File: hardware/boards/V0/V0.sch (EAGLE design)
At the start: 157 parts, among them IC2 TPS6300, J12 3.5mm TRRS Jack, J2 HIROSE_DM3BT-DSF-PEJSHIROSE_D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, J3 MOLEX_105450-0101MOLEX_105450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, Q2 ON_SEMI_MMBT5551LT1GON_SEMI_M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, U1 VS1053-L, U2 MICROCHIP_MCP73831T-2ATI-OTMI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, X3 FH12-45S-0.5SH

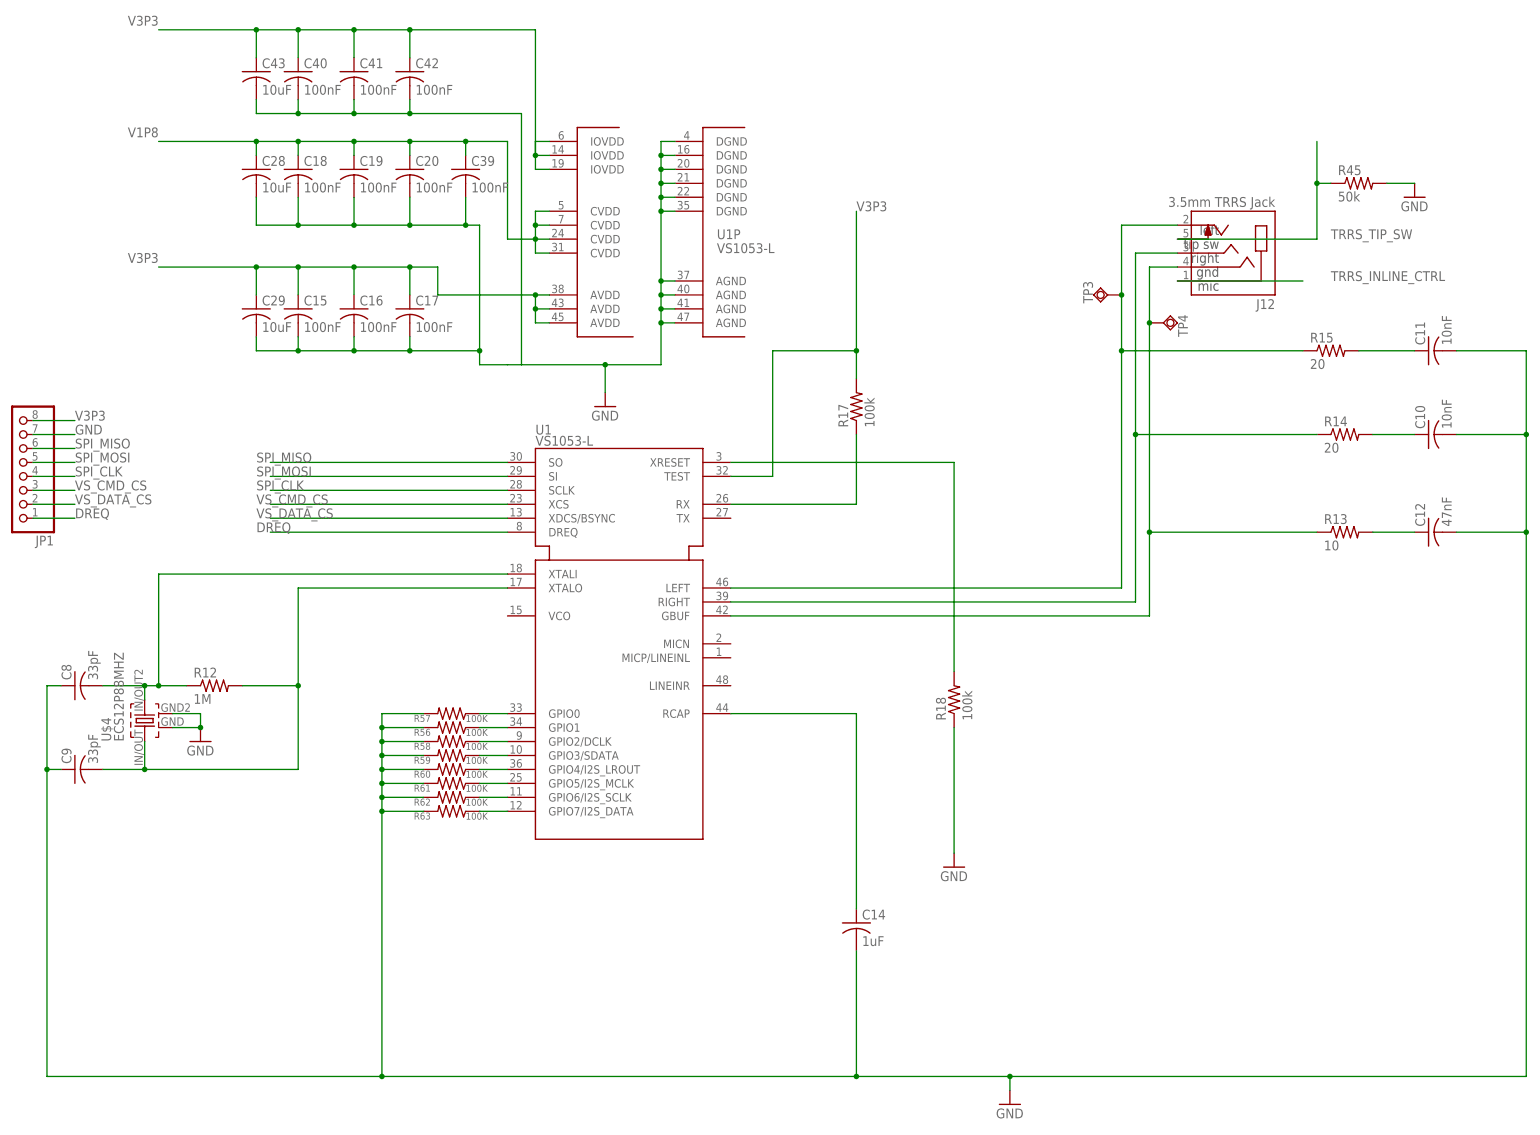
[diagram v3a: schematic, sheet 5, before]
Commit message: VS1053 changes
Switch back to bridging all the GPIO pins (the datasheet's sample connection diagram has it wired this way, so it'll hopefully not be an issue) and tie xRESET to V3P3 (pull-up) so that we can actually boot.
The Adafruit VS1053 breakout schematic mentions that they tie xRESET to low (pull-down) to avoid transients (clicks) in the headphone outputs (as per [this](http://www.vlsi.fi/uploads/media/vs10XXan.pdf)) - making the MCU enable the VS1053 some time after system power up apparently helps mitigate this. Adafruit goes a step further and says that not doing this can "damage the earphones", but since we're pretty heavily pin starved we'll have to risk it.

At this point we seem to match Adafruit's VS1053 breakout in most of the relevant ways. The main (relevant) differences are that we don't differentiate between AGND and GND (or have ferrite beads between them), don't have pull-ups on our CS pins (though this is probably okay since the ESP32 [supposedly doesn't need external pull-ups on its SPI CS pins](https://esp32.com/viewtopic.php?t=3650)), don't have the 2nd set of capacitors/resistors on our right/left output lines (ESD?), and don't have what looks to be a bypass cap and a pull-up (??) resistor on xRESET (peculiar since there's a pull-down resistor on the other side of the level shifter for this pin).

Anyways, we should be in decent shape and we've got the header pins as an escape hatch in case things don't work out.
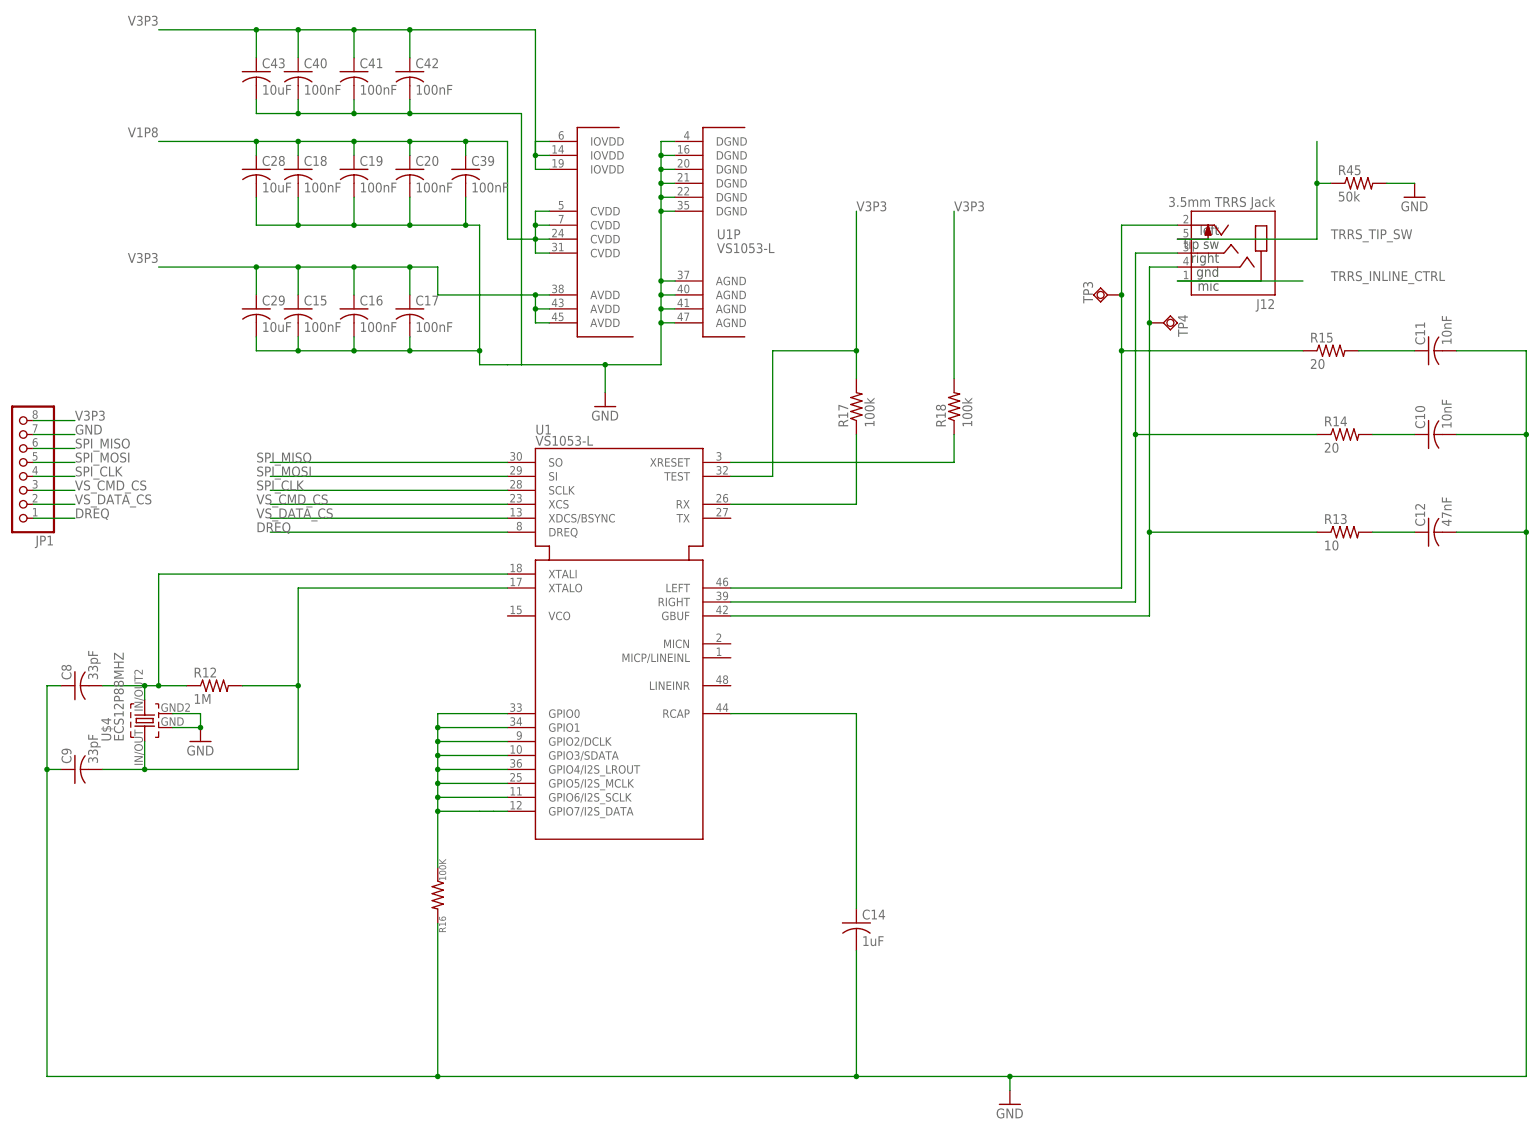
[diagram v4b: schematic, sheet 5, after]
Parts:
- removed R56, R57, R58, R59, R60, R61, R62, R63: 100K, rcl:R-US_R0402
- added R16: 100K, rcl:R-US_R0402
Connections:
- removed net N$13: R58.1, U1G$1.GPIO2/DCLK
- removed net N$15: R59.1, U1G$1.GPIO3/SDATA
- removed net N$17: R60.1, U1G$1.GPIO4/I2S_LROUT
- removed net N$38: R61.1, U1G$1.GPIO5/I2S_MCLK
- removed net N$44: R62.1, U1G$1.GPIO6/I2S_SCLK
- removed net N$7: R57.1, U1G$1.GPIO0
- removed net N$9: R56.1, U1G$1.GPIO1
- net GND: now also R16.2; no longer R18.1, R56.2, R57.2, R58.2, R59.2, R60.2, R61.2, R62.2, R63.2
- net N$41: now also R18.1; no longer R18.2
- net N$45: now also R16.1, U1G$1.GPIO0, U1G$1.GPIO1, U1G$1.GPIO2/DCLK, U1G$1.GPIO3/SDATA, U1G$1.GPIO4/I2S_LROUT, U1G$1.GPIO5/I2S_MCLK, U1G$1.GPIO6/I2S_SCLK; no longer R63.1
- net V3P3: now also R18.2
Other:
- moved on the sheet: R18
